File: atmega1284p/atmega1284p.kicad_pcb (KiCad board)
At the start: 2 copper layers, 48.3 x 99.1 mm, 38 parts, among them J1 PA, J10 AVR-ISP-6, J11 USB_B_Mini, J12 CC1101_Breakout, J2 PB, J3 PC, J4 PD, J5 I2C1, J6 I2C2, J7 Power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

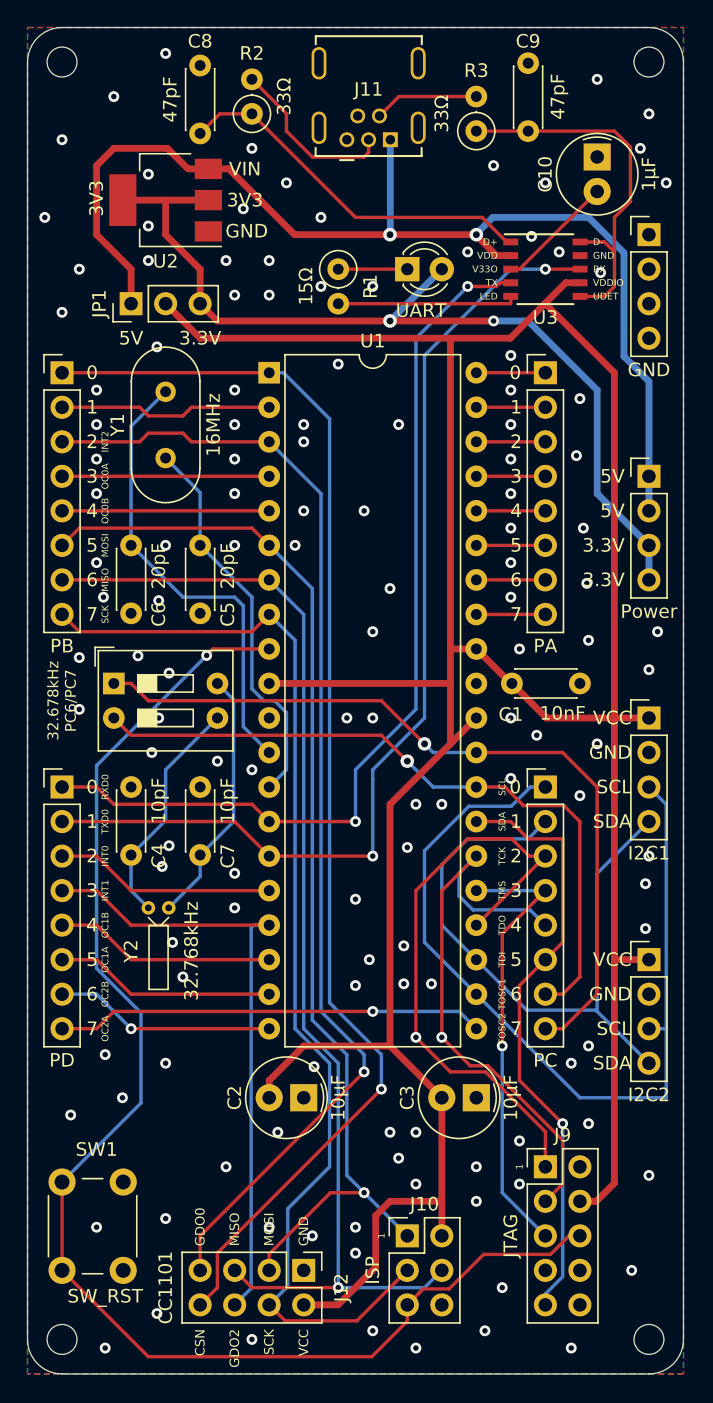
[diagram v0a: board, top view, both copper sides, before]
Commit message: atmega1284p: Use 12MHz crystal and 3.3V
This way the board is safe to used with the CC1101
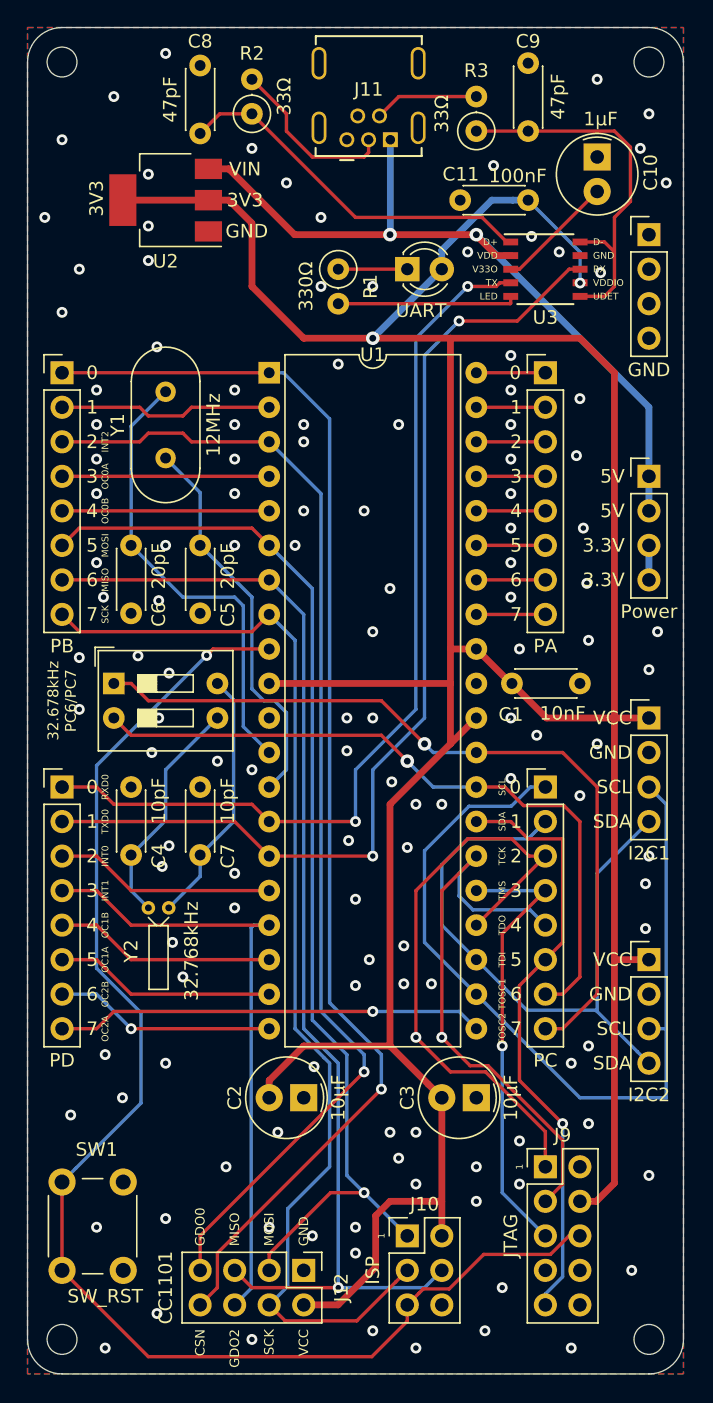
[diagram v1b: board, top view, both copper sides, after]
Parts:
- removed JP1: Jumper_Power, Connector_PinHeader_2.54mm:PinHeader_1x03_P2.54mm_Vertical
- added C11: 100nF, Capacitor_THT:C_Disc_D4.3mm_W1.9mm_P5.00mm, F.Cu at (141.0, 66.0)
- R1: value 15Ω -> 330Ω
- Y1: value 16MHz -> 12MHz
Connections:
- D1 pad 2: +3V3 -> VCC
- U2 pad 2: +3V3 -> VCC
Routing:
- net +3V3: track 67.7 -> 2.54 mm, vias 2 -> 0
- net VCC: track 234.7 -> 262.5 mm, vias 0 -> 2
- net +5V: track 84.8 -> 57.5 mm
- net GND: vias 135 -> 132
